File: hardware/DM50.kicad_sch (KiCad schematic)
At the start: 111 parts, among them J1 ST-LINK, J2 USB_C_Receptacle_USB2.0_14P, J4 LiPO 3,7V, Q1 MMBT3904, SW1 SW_SPST, SW10 BT_SMD, SW11 BT_SMD, SW12 BT_SMD, SW13 BT_SMD, SW14 BT_SMD, SW15 BT_SMD, SW16 BT_SMD, SW17 BT_SMD, SW18 BT_SMD, SW19 BT_SMD, SW2 BT_SMD, SW20 BT_SMD, SW21 BT_SMD, SW22 BT_SMD, SW23 BT_SMD, SW24 BT_SMD, SW25 BT_SMD, SW26 BT_SMD, SW27 BT_SMD, SW28 BT_SMD, SW29 BT_SMD, SW3 BT_SMD, SW30 BT_SMD, SW31 BT_SMD, SW32 BT_SMD, SW33 BT_SMD, SW34 BT_SMD, SW35 BT_SMD, SW36 BT_SMD, SW37 BT_SMD, SW38 BT_SMD, SW39 BT_SMD, SW4 BT_SMD, SW40 BT_SMD, SW41 BT_SMD, SW42 SW_SPST, SW43 BT_SMD, SW44 BT_SMD, SW45 BT_SMD, SW46 BT_SMD, SW47 BT_SMD, SW48 BT_SMD, SW49 BT_SMD, SW5 BT_SMD, SW50 BT_SMD, SW51 BT_SMD, SW52 BT_SMD, SW6 BT_SMD, SW7 BT_SMD, SW8 BT_SMD, SW9 BT_SMD, U1 EA_DOGL128X-6, U2 STM32U575CITx, U3 W25Q128JVSIQ, U4 USBLC6-2SC6, U5 ADP2108AUJ-3.3, U6 MCP73831, Y1 32768

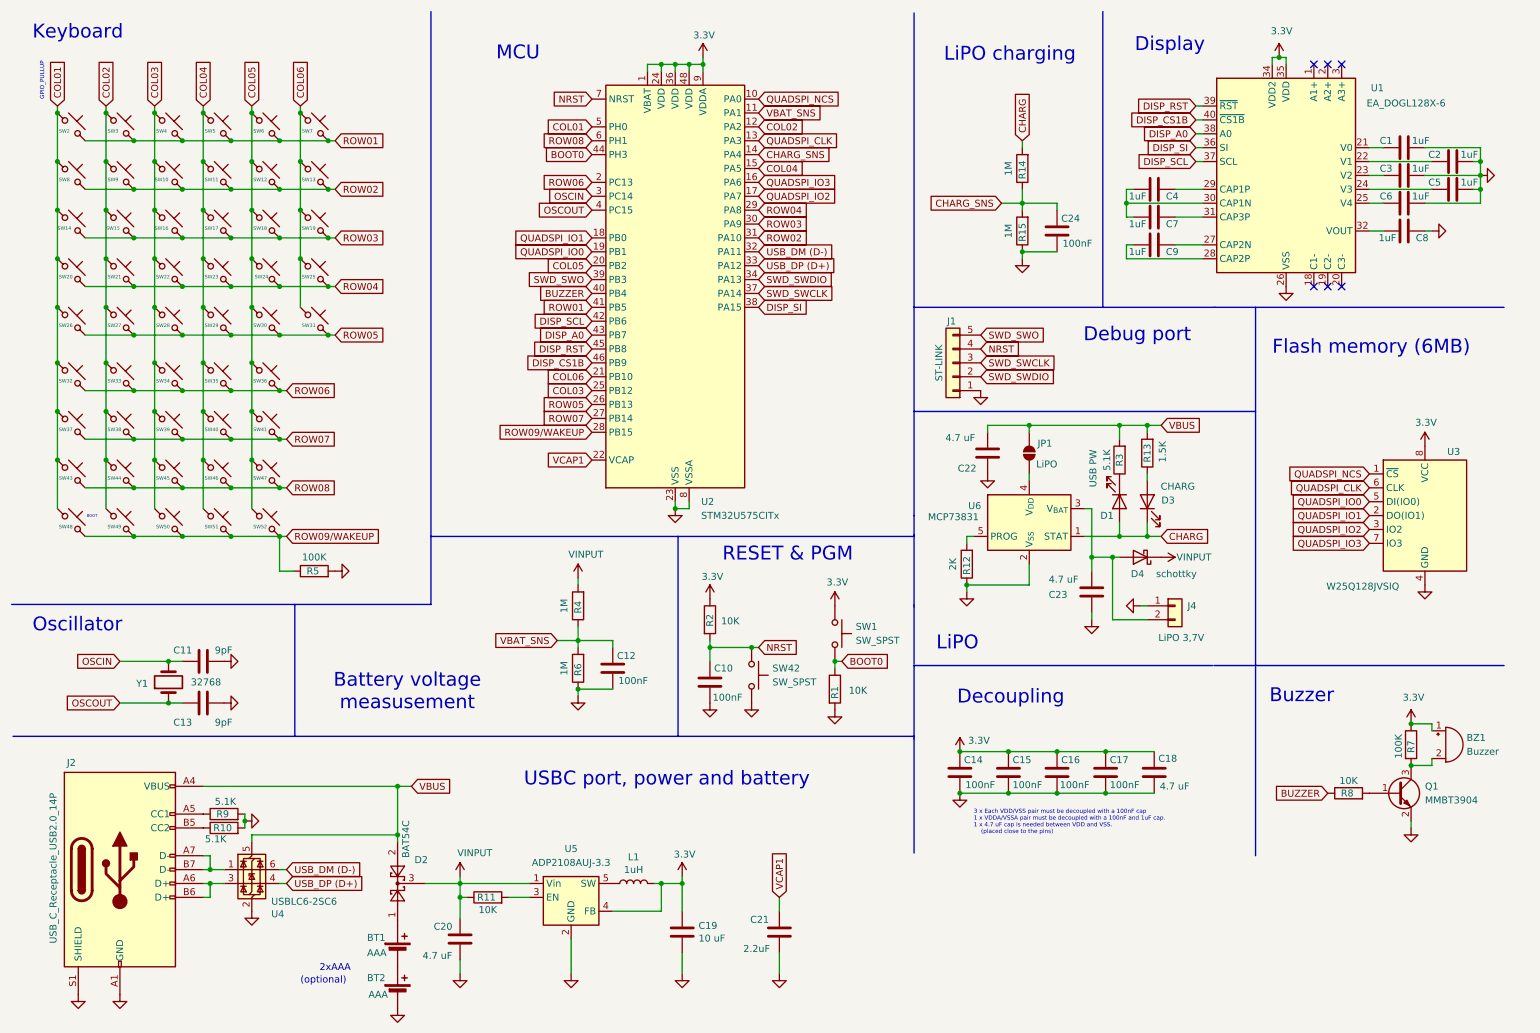
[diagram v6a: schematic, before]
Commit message: STM32U575RIT6 change
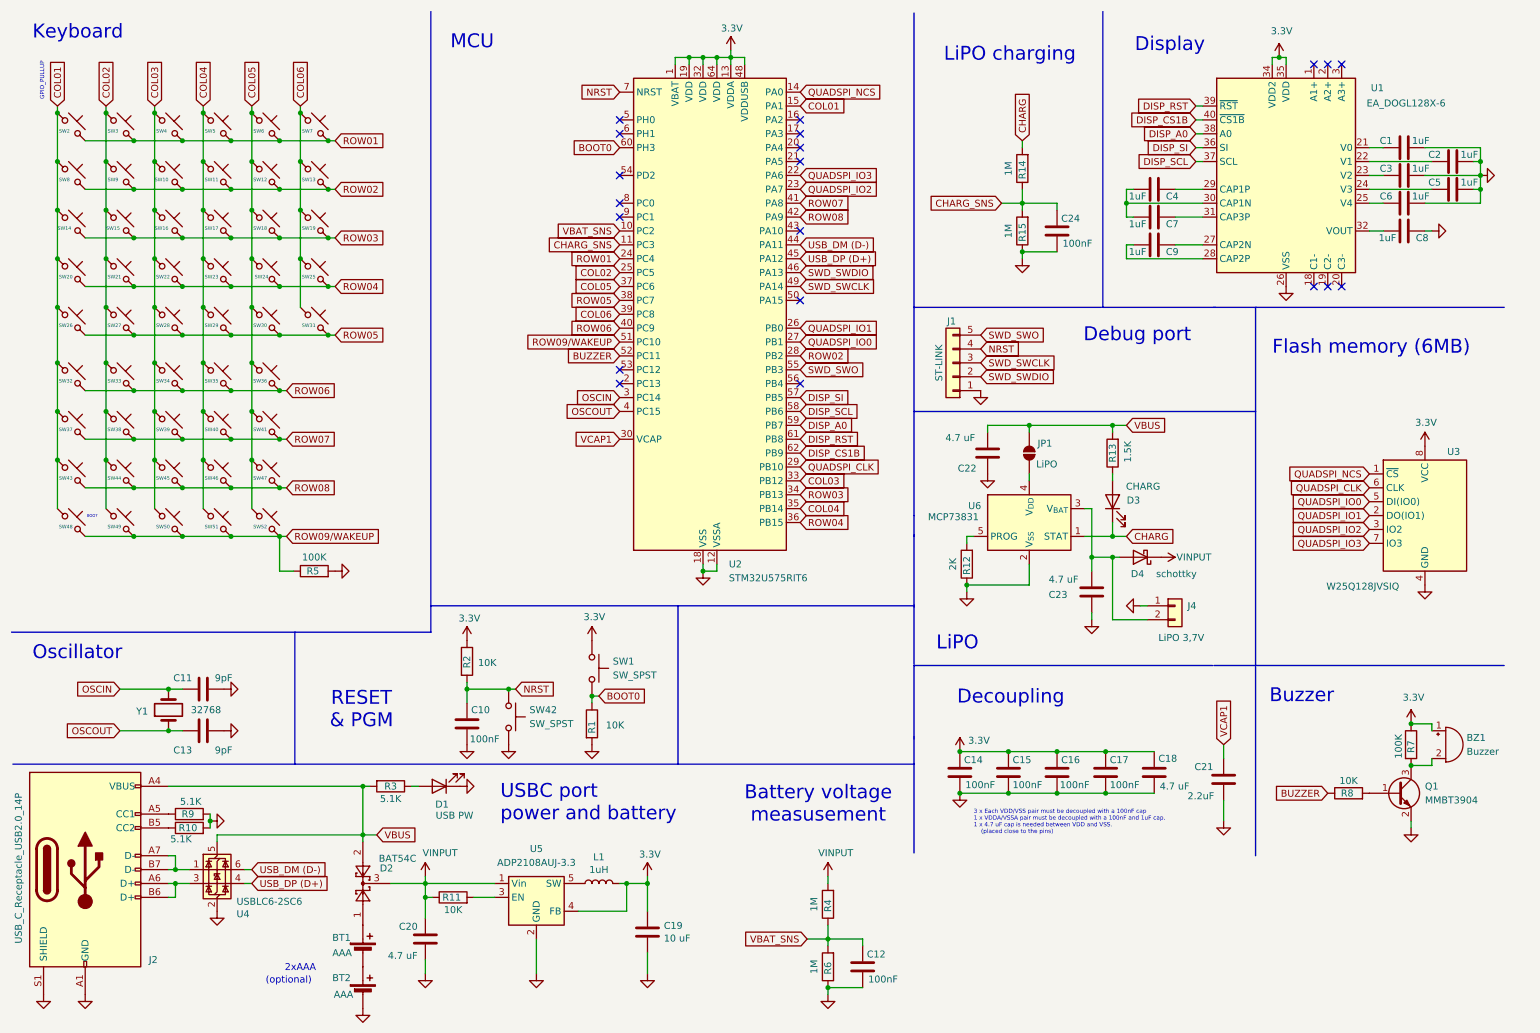
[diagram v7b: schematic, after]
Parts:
- removed U2: STM32U575CITx, Package_QFP:LQFP-48_7x7mm_P0.5mm, symbol MCU_ST_STM32U5:STM32U575CITx
- added U2: STM32U575RIT6, Package_QFP:LQFP-64_10x10mm_P0.5mm, symbol MCU_ST_STM32U5:STM32U575RITx
- D4: LCSC (none) -> C179319
- J4: LCSC (none) -> C173752
- U3: LCSC (none) -> C97521
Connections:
- net 3.3V: now also U2.1 (VBAT), U2.13 (VDDA), U2.19 (VDD), U2.32 (VDD), U2.48 (VDDUSB), U2.64 (VDD)
- net BOOT0: now also U2.60 (PH3)
- net BUZZER: now also U2.52 (PC11)
- net CHARG: no longer D1.2 (A)
- net CHARG_SNS: now also U2.11 (PC3)
- net COL01: now also U2.15 (PA1)
- net COL02: now also U2.25 (PC5)
- net COL03: now also U2.33 (PB12)
- net COL04: now also U2.35 (PB14)
- net COL05: now also U2.37 (PC6)
- net COL06: now also U2.39 (PC8)
- net DISP_A0: now also U2.59 (PB7)
- net DISP_CS1B: now also U2.62 (PB9)
- net DISP_RST: now also U2.61 (PB8)
- net DISP_SCL: now also U2.58 (PB6)
- net DISP_SI: now also U2.57 (PB5)
- net GND: now also D1.1 (K), U2.12 (VSSA), U2.18 (VSS), U2.31 (VSS), U2.47 (VSS), U2.63 (VSS)
- net NRST: now also U2.7 (NRST)
- net OSCIN: now also U2.3 (PC14)
- net OSCOUT: now also U2.4 (PC15)
- net QUADSPI_CLK: now also U2.29 (PB10)
- net QUADSPI_IO0: now also U2.27 (PB1)
- net QUADSPI_IO1: now also U2.26 (PB0)
- net QUADSPI_IO2: now also U2.23 (PA7)
- net QUADSPI_IO3: now also U2.22 (PA6)
- net QUADSPI_NCS: now also U2.14 (PA0)
- net ROW01: now also U2.24 (PC4)
- net ROW02: now also U2.28 (PB2)
- net ROW03: now also U2.34 (PB13)
- net ROW04: now also U2.36 (PB15)
- net ROW05: now also U2.38 (PC7)
- net ROW06: now also U2.40 (PC9)
- net ROW07: now also U2.41 (PA8)
- net ROW08: now also U2.42 (PA9)
- net ROW09/WAKEUP: now also U2.51 (PC10)
- net SWD_SWCLK: now also U2.49 (PA14)
- net SWD_SWDIO: now also U2.46 (PA13)
- net SWD_SWO: now also U2.55 (PB3)
- net USB_DM (D-): now also U2.44 (PA11)
- net USB_DP (D+): now also U2.45 (PA12)
- net VBAT_SNS: now also U2.10 (PC2)
- net VCAP1: now also U2.30 (VCAP)
- net at R3.1: now also D1.2 (A); no longer D1.1 (K)
- no-connect marks 6 -> 20
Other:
- note added: "USBC port power and battery"
- note removed: "USBC port, power and battery"
- moved on the sheet: BT1, BT2, C10, C11, C12, C13, C19, C20, C21, D1, D2, D3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

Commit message: PCB CHANGES
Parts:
- added J3: SERIAL, DM50:SAMTEC-SMH-105-02-X-S, symbol Connector_Generic:Conn_01x05
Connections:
- net 3.3V: now also J3.5 (Pin_5)
- net GND: now also J3.1 (Pin_1)
- net USART_TX: now reaches U2.16 (PA2)
- net USART_TX: now also J3.4 (Pin_4)
- net USART_RX: now reaches U2.17 (PA3)
- net USART_RX: now also J3.3 (Pin_3)
- net ADC_IN: now reaches U2.8 (PC0)
- net ADC_IN: now also J3.2 (Pin_2)
- no-connect marks 20 -> 17
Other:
- note added: "Serial port"
